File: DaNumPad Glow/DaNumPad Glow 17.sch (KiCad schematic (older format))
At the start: 27 parts, among them J1 USB_C_Receptacle_USB2.0, J4 Conn_01x06, SW24 TS-A002, U1 SRV05-4, U5 ATmega32U4, X2 X322516MLB4SI

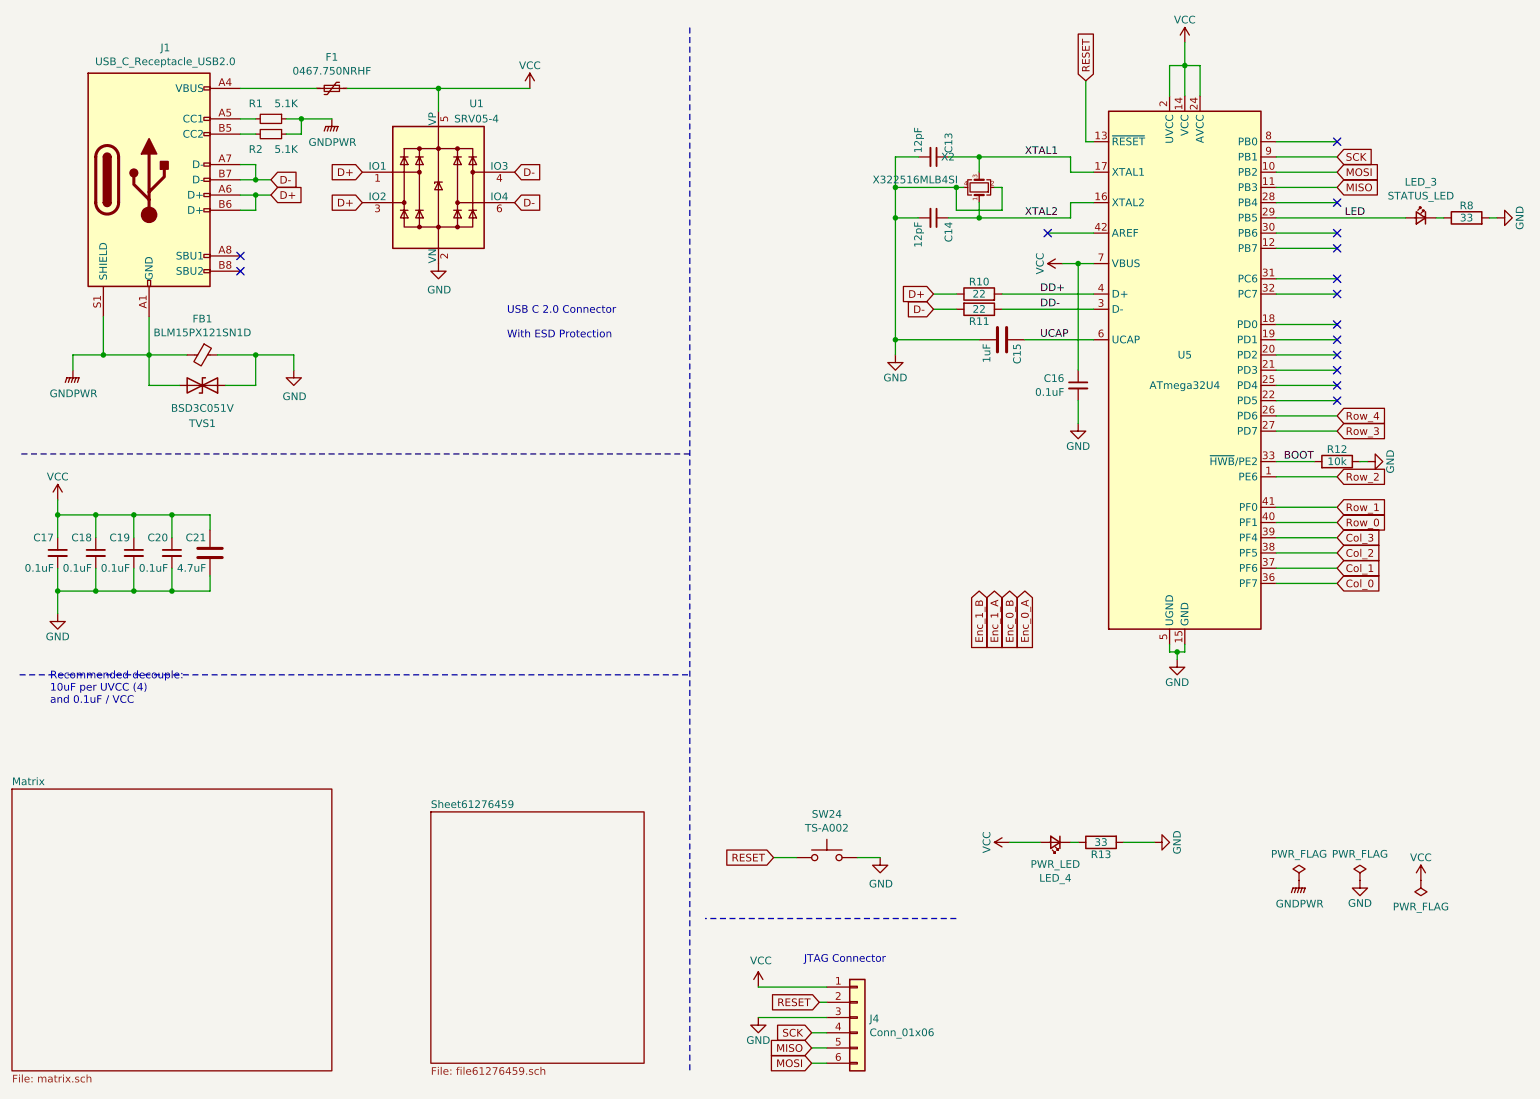
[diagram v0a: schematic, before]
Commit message: Glow version redesign
For now, it's 17 keys only.
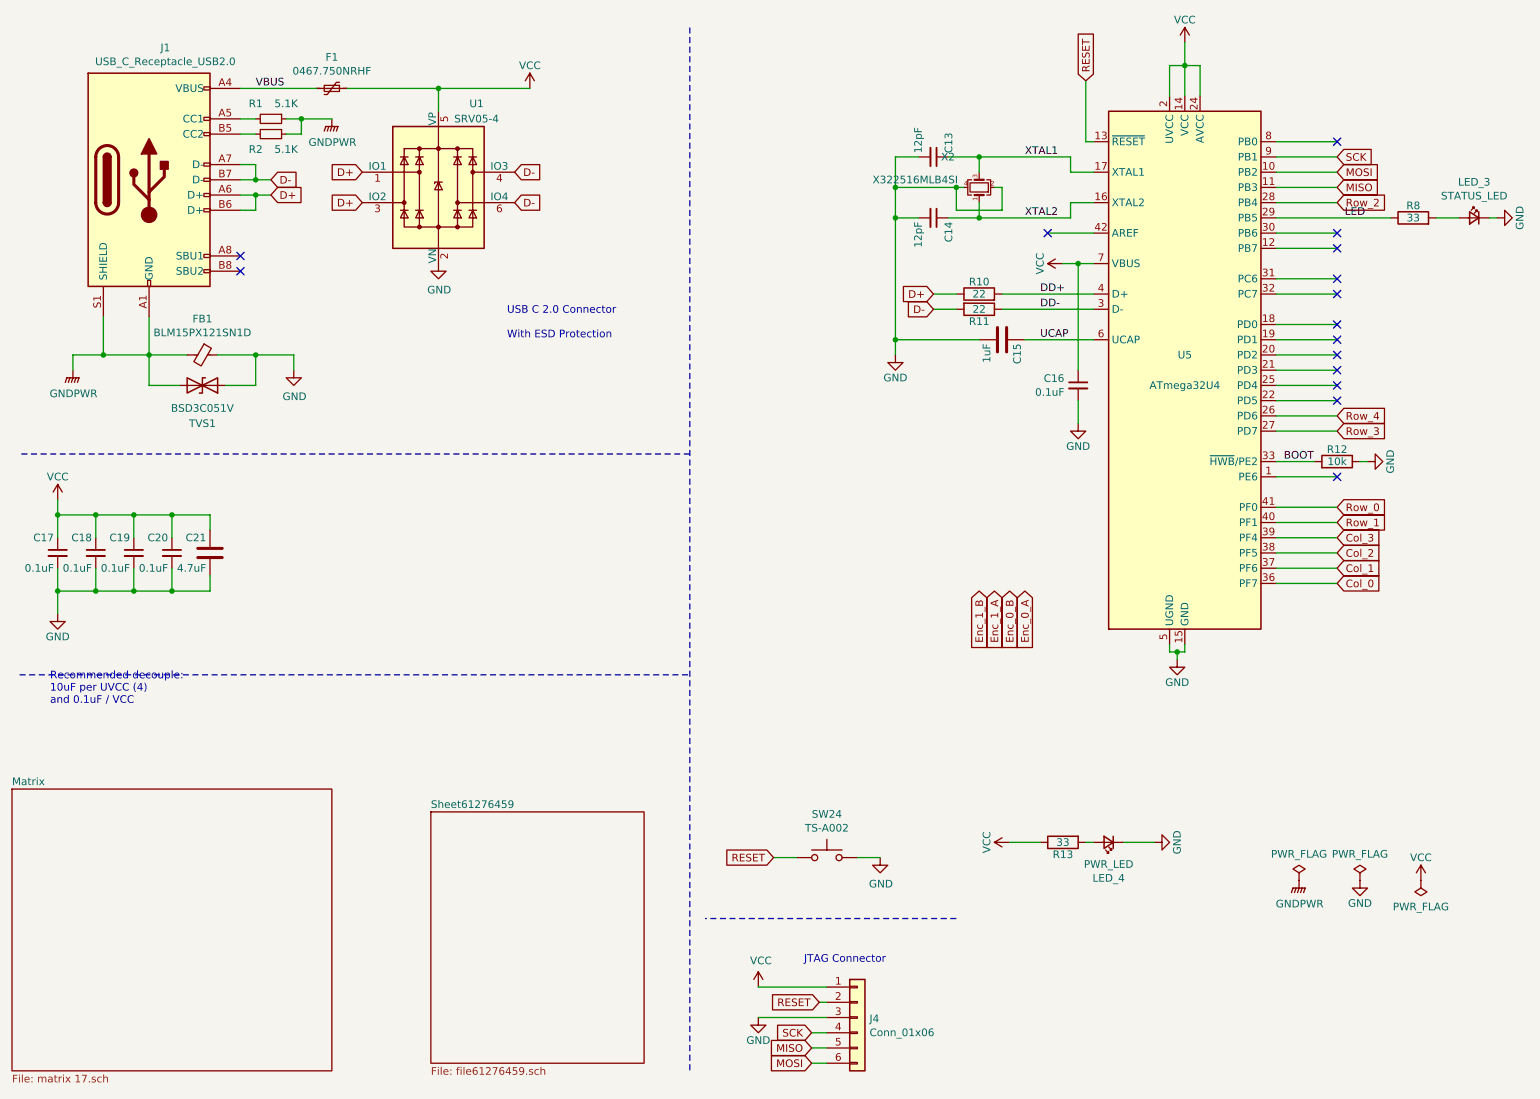
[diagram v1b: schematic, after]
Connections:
- net GND: now also LED_3.1 (K), LED_4.1 (K); no longer R13.2, R8.2
- net LED: now also R8.1; no longer LED_3.2 (A)
- net Row_0: now also U5.41 (PF0); no longer U5.40 (PF1)
- net Row_1: now also U5.40 (PF1); no longer U5.41 (PF0)
- net Row_2: now also U5.28 (PB4); no longer U5.1 (PE6)
- net VCC: now also R13.1; no longer LED_4.2 (A)
- net VBUS: now reaches F1.2, J1.A4 (VBUS), J1.A9 (VBUS), J1.B4 (VBUS), J1.B9 (VBUS)
- new net: LED_3.2 (A), R8.2
- new net: LED_4.2 (A), R13.2
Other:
- moved on the sheet: LED_3, LED_4, R13, R8
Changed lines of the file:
@@
 Text GLabel 9350 4050 2    50   Input ~ 0
 Col_3
+Text GLabel 9350 3850 2    50   Input ~ 0
+Row_0
 Text GLabel 9350 3950 2    50   Input ~ 0
-Row_0
-Text GLabel 9350 3850 2    50   Input ~ 0
 Row_1
-Text GLabel 9350 3650 2    50   Input ~ 0
+Text GLabel 9350 1850 2    50   Input ~ 0
 Row_2
 Text GLabel 9350 3350 2    50   Input ~ 0
@@
 U 6159EE28
 F0 "Matrix" 50
-F1 "matrix.sch" 50
+F1 "matrix 17.sch" 50
 $EndSheet
 Text GLabel 7300 4400 3    50   Input ~ 0
@@
 Wire Wire Line
 	9350 1850 8950 1850
-NoConn ~ 9350 1850
 Wire Wire Line
 	9350 2050 8950 2050
@@
 Text Label 9400 1950 0    50   ~ 0
 LED
-Wire Wire Line
-	9800 1950 8950 1950
 $Comp
 L power:GND #PWR?
@@
 L Device:LED_Small LED_?
 U 1 1 612C1842
-P 9900 1950
+P 10250 1950
 AR Path="/60039BC8/612C1842" Ref="LED_?"  Part="1"
 AR Path="/612C1842" Ref="LED_3"  Part="1"
-F 0 "LED_3" H 9900 2185 50  0000 C CNN
-F 1 "STATUS_LED" H 9900 2094 50  0000 C CNN
-F 2 "LED_SMD:LED_0603_1608Metric" V 9900 1950 50  0001 C CNN
-F 3 "~" V 9900 1950 50  0001 C CNN
-F 4 "1" H 9900 1950 50  0001 C CNN "Fält4"
-F 5 "Hubei KENTO Elec" H 9900 1950 50  0001 C CNN "Manufacturer_Name"
-F 6 "KT-0603R" H 9900 1950 50  0001 C CNN "Manufacturer_Part_Number"
-F 7 "604-APT1608EC" H 9900 1950 50  0001 C CNN "Mouser Part Number"
-F 8 "C2286" H 9900 1950 50  0001 C CNN "JLPCB Part #"
-F 9 "Basic" H 9900 1950 50  0001 C CNN "JLPCB Type"
-	1    9900 1950
+F 0 "LED_3" H 10250 2185 50  0000 C CNN
+F 1 "STATUS_LED" H 10250 2094 50  0000 C CNN
+F 2 "LED_SMD:LED_0603_1608Metric" V 10250 1950 50  0001 C CNN
+F 3 "~" V 10250 1950 50  0001 C CNN
+F 4 "1" H 10250 1950 50  0001 C CNN "Fält4"
+F 5 "Hubei KENTO Elec" H 10250 1950 50  0001 C CNN "Manufacturer_Name"
+F 6 "KT-0603R" H 10250 1950 50  0001 C CNN "Manufacturer_Part_Number"
+F 7 "604-APT1608EC" H 10250 1950 50  0001 C CNN "Mouser Part Number"
+F 8 "C2286" H 10250 1950 50  0001 C CNN "JLPCB Part #"
+F 9 "Basic" H 10250 1950 50  0001 C CNN "JLPCB Type"
+	1    10250 1950
 	-1   0    0    -1
 $EndComp
@@
 L Device:R R?
 U 1 1 612C184E
-P 10200 1950
+P 9850 1950
 AR Path="/5D8219F0/612C184E" Ref="R?"  Part="1"
 AR Path="/5D6CC2CC/612C184E" Ref="R?"  Part="1"
@@
 AR Path="/60039BC8/612C184E" Ref="R?"  Part="1"
 AR Path="/612C184E" Ref="R8"  Part="1"
-F 0 "R8" V 10280 1950 50  0000 C CNN
-F 1 "33" V 10200 1950 50  0000 C CNN
-F 2 "Resistor_SMD:R_0603_1608Metric" V 10130 1950 50  0001 C CNN
-F 3 "" H 10200 1950 50  0001 C CNN
-F 4 "1" H 10200 1950 50  0001 C CNN "Fält4"
-F 5 "Uniroyal Elec" H 10200 1950 50  0001 C CNN "Manufacturer_Name"
-F 6 "0603WAF330JT5E" H 10200 1950 50  0001 C CNN "Manufacturer_Part_Number"
-F 7 "667-ERJ-3EKF33R0V" H 10200 1950 50  0001 C CNN "Mouser Part Number"
-F 8 "C23140" H 10200 1950 50  0001 C CNN "JLPCB Part #"
-F 9 "Basic" H 10200 1950 50  0001 C CNN "JLPCB Type"
-	1    10200 1950
+F 0 "R8" V 9930 1950 50  0000 C CNN
+F 1 "33" V 9850 1950 50  0000 C CNN
+F 2 "Resistor_SMD:R_0603_1608Metric" V 9780 1950 50  0001 C CNN
+F 3 "" H 9850 1950 50  0001 C CNN
+F 4 "1" H 9850 1950 50  0001 C CNN "Fält4"
+F 5 "Uniroyal Elec" H 9850 1950 50  0001 C CNN "Manufacturer_Name"
+F 6 "0603WAF330JT5E" H 9850 1950 50  0001 C CNN "Manufacturer_Part_Number"
+F 7 "667-ERJ-3EKF33R0V" H 9850 1950 50  0001 C CNN "Mouser Part Number"
+F 8 "C23140" H 9850 1950 50  0001 C CNN "JLPCB Part #"
+F 9 "Basic" H 9850 1950 50  0001 C CNN "JLPCB Type"
+	1    9850 1950
 	0    -1   -1   0
 $EndComp
 Wire Wire Line
-	10050 1950 10000 1950
+	10150 1950 10000 1950
 Wire Wire Line
 	9350 2150 8950 2150
@@
 	0    -1   -1   0
 $EndComp
-Wire Wire Line
-	7650 6050 7600 6050
 $Comp
 L Device:R R?
 U 1 1 612F758E
-P 7800 6050
+P 7550 6050
 AR Path="/5D8219F0/612F758E" Ref="R?"  Part="1"
 AR Path="/5D6CC2CC/612F758E" Ref="R?"  Part="1"
@@
 AR Path="/612F758E" Ref="R13"  Part="1"
 AR Path="/61263053/612F758E" Ref="R?"  Part="1"
-F 0 "R13" V 7880 6050 50  0000 C CNN
-F 1 "33" V 7800 6050 50  0000 C CNN
-F 2 "Resistor_SMD:R_0603_1608Metric" V 7730 6050 50  0001 C CNN
-F 3 "" H 7800 6050 50  0001 C CNN
-F 4 "1" H 7800 6050 50  0001 C CNN "Fält4"
-F 5 "Uniroyal Elec" H 7800 6050 50  0001 C CNN "Manufacturer_Name"
-F 6 "0603WAF330JT5E" H 7800 6050 50  0001 C CNN "Manufacturer_Part_Number"
-F 7 "667-ERJ-3EKF33R0V" H 7800 6050 50  0001 C CNN "Mouser Part Number"
-F 8 "C23140" H 7800 6050 50  0001 C CNN "JLPCB Part #"
-F 9 "Basic" H 7800 6050 50  0001 C CNN "JLPCB Type"
-	1    7800 6050
+F 0 "R13" V 7630 6050 50  0000 C CNN
+F 1 "33" V 7550 6050 50  0000 C CNN
+F 2 "Resistor_SMD:R_0603_1608Metric" V 7480 6050 50  0001 C CNN
+F 3 "" H 7550 6050 50  0001 C CNN
+F 4 "1" H 7550 6050 50  0001 C CNN "Fält4"
+F 5 "Uniroyal Elec" H 7550 6050 50  0001 C CNN "Manufacturer_Name"
+F 6 "0603WAF330JT5E" H 7550 6050 50  0001 C CNN "Manufacturer_Part_Number"
+F 7 "667-ERJ-3EKF33R0V" H 7550 6050 50  0001 C CNN "Mouser Part Number"
+F 8 "C23140" H 7550 6050 50  0001 C CNN "JLPCB Part #"
+F 9 "Basic" H 7550 6050 50  0001 C CNN "JLPCB Type"
+	1    7550 6050
 	0    -1   1    0
 $EndComp
@@
 L Device:LED_Small LED_?
 U 1 1 612F759A
-P 7500 6050
+P 7850 6050
 AR Path="/60039BC8/612F759A" Ref="LED_?"  Part="1"
 AR Path="/612F759A" Ref="LED_4"  Part="1"
 AR Path="/61263053/612F759A" Ref="LED_?"  Part="1"
-F 0 "LED_4" H 7500 6285 50  0000 C CNN
-F 1 "PWR_LED" H 7500 6194 50  0000 C CNN
-F 2 "LED_SMD:LED_0603_1608Metric" V 7500 6050 50  0001 C CNN
-F 3 "~" V 7500 6050 50  0001 C CNN
-F 4 "1" H 7500 6050 50  0001 C CNN "Fält4"
-F 5 "Hubei KENTO Elec" H 7500 6050 50  0001 C CNN "Manufacturer_Name"
-F 6 "KT-0603R" H 7500 6050 50  0001 C CNN "Manufacturer_Part_Number"
-F 7 "604-APT1608EC" H 7500 6050 50  0001 C CNN "Mouser Part Number"
-F 8 "C2286" H 7500 6050 50  0001 C CNN "JLPCB Part #"
-F 9 "Basic" H 7500 6050 50  0001 C CNN "JLPCB Type"
-	1    7500 6050
+F 0 "LED_4" H 7850 6285 50  0000 C CNN
+F 1 "PWR_LED" H 7850 6194 50  0000 C CNN
+F 2 "LED_SMD:LED_0603_1608Metric" V 7850 6050 50  0001 C CNN
+F 3 "~" V 7850 6050 50  0001 C CNN
+F 4 "1" H 7850 6050 50  0001 C CNN "Fält4"
+F 5 "Hubei KENTO Elec" H 7850 6050 50  0001 C CNN "Manufacturer_Name"
+F 6 "KT-0603R" H 7850 6050 50  0001 C CNN "Manufacturer_Part_Number"
+F 7 "604-APT1608EC" H 7850 6050 50  0001 C CNN "Mouser Part Number"
+F 8 "C2286" H 7850 6050 50  0001 C CNN "JLPCB Part #"
+F 9 "Basic" H 7850 6050 50  0001 C CNN "JLPCB Type"
+	1    7850 6050
 	-1   0    0    1
 $EndComp
@@
 F1 "file61276459.sch" 50
 $EndSheet
+Text Label 2250 1100 0    50   ~ 0
+VBUS
+Wire Wire Line
+	9700 1950 8950 1950
+Wire Wire Line
+	7750 6050 7700 6050
+NoConn ~ 9350 3650
 $EndSCHEMATC

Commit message: Cleanup of silkscreen
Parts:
- C1: renamed from C13; Fält4 1 -> (none); JLPCB Part # C38523 -> (none); LCSC (none) -> C38523
- C2: renamed from C14; Fält4 1 -> (none); JLPCB Part # C38523 -> (none); LCSC (none) -> C38523
- C3: renamed from C15; Fält4 1 -> (none); JLPCB Part # C28323 -> (none); LCSC (none) -> C28323
- C4: renamed from C16; value 0.1uF -> 100nF; Fält4 1 -> (none); JLPCB Part # C14663 -> (none); LCSC (none) -> C14663
- C5: renamed from C17; value 0.1uF -> 100nF; Fält4 1 -> (none); JLPCB Part # C14663 -> (none); LCSC (none) -> C14663
- C6: renamed from C18; value 0.1uF -> 100nF; Fält4 1 -> (none); JLPCB Part # C14663 -> (none); LCSC (none) -> C14663
- C7: renamed from C19; value 0.1uF -> 100nF; Fält4 1 -> (none); JLPCB Part # C14663 -> (none); LCSC (none) -> C14663
- C8: renamed from C20; value 0.1uF -> 100nF; Fält4 1 -> (none); JLPCB Part # C14663 -> (none); LCSC (none) -> C14663
- C9: renamed from C21; Fält4 1 -> (none); JLPCB Part # C1779 -> (none); LCSC (none) -> C1779
- F1, J1, TVS1: JLPCB Type (none) -> Extended
- FB1: JLPCB Type (none) -> Extended; LCSC C882964 -> C88970
- J2: renamed from J4; Fält4 0 -> (none); fit_field (none) -> DNF
- LED_1: renamed from LED_3; Fält4 1 -> (none); JLPCB Part # C2286 -> (none); LCSC (none) -> C2286
- LED_2: renamed from LED_4; Fält4 1 -> (none); JLPCB Part # C2286 -> (none); LCSC (none) -> C2286
- R1, R2, U1: JLPCB Type (none) -> Basic
- R3: renamed from R8; Fält4 1 -> (none); JLPCB Part # C23140 -> (none); LCSC (none) -> C23140
- R4: renamed from R10; Fält4 1 -> (none); JLPCB Part # C23345 -> (none); LCSC (none) -> C23345
- R5: renamed from R11; Fält4 1 -> (none); JLPCB Part # C23345 -> (none); LCSC (none) -> C23345
- R6: renamed from R12; Fält4 1 -> (none); JLPCB Part # C25804 -> (none); LCSC (none) -> C25804
- R7: renamed from R13; Fält4 1 -> (none); JLPCB Part # C23140 -> (none); LCSC (none) -> C23140
- SW1: renamed from SW24; fit_field (none) -> DNF
- U2: renamed from U5; Fält4 1 -> (none); JLPCB Part # C112161 -> (none); LCSC (none) -> C112161
- X1: renamed from X2; Fält4 1 -> (none); JLPCB Part # C13738 -> (none); LCSC (none) -> C13738
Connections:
- net RGB: now reaches U2.1 (PE6)
- no-connect marks 15 -> 14
